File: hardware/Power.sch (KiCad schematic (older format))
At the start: 30 parts, among them J8 Batt, Q10 AO3401A, Q11 AO3400 (A09T), Q12 AO3401A, Q13 AO3400 (A09T), Q14 AO3400 (A09T), Q9 AO3400 (A09T), U1 TP4056, U3 DW-01, U8 HX9193-33GB

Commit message: Wrover fp
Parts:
- C15: LCSC (none) -> C14663
- C16, C22: LCSC (none) -> C15849
- C24, C25: LCSC (none) -> C134722
- D17, D18: LCSC (none) -> C72043
- D19: LCSC (none) -> C2480
- Q10, Q12: LCSC (none) -> C15127
- Q11, Q13, Q14, Q9: LCSC (none) -> C20917
- R47, R48, R52, R53: LCSC (none) -> C25804
- R49, R50, R51: LCSC (none) -> C22765
- R54: LCSC (none) -> C23179
- R55: LCSC (none) -> C21190
- R57: LCSC (none) -> C21189
- U1: LCSC (none) -> C16581
- U3: LCSC (none) -> C14213
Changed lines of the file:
@@
 F 7 "Eldon Vloerstaande kasten DW - DW01" H 6700 4050 50  0001 L BNN "Field7"
 F 8 "DW01" H 6700 4050 50  0001 L BNN "Field8"
+F 9 "C14213" H 6700 4050 50  0001 C CNN "LCSC"
 	1    6700 4050
 	1    0    0    -1
@@
 F 2 "Resistor_SMD:R_0603_1608Metric" V 5730 3800 50  0001 C CNN
 F 3 "~" H 5800 3800 50  0001 C CNN
+F 4 "C23179" H 5800 3800 50  0001 C CNN "LCSC"
 	1    5800 3800
 	0    1    1    0
@@
 F 2 "Capacitor_SMD:C_0603_1608Metric" H 6188 3800 50  0001 C CNN
 F 3 "~" H 6150 3950 50  0001 C CNN
+F 4 "C14663" H 6150 3950 50  0001 C CNN "LCSC"
 	1    6150 3950
 	1    0    0    -1
@@
 F 2 "Package_TO_SOT_SMD:SOT-23" H 6650 4775 50  0001 L CIN
 F 3 "http://www.aosmd.com/pdfs/datasheet/ao3400.pdf" H 6450 4850 50  0001 L CNN
+F 4 "C20917" H 6450 4850 50  0001 C CNN "LCSC"
 	1    6450 4850
 	0    1    1    0
@@
 F 2 "Package_TO_SOT_SMD:SOT-23" H 7100 4775 50  0001 L CIN
 F 3 "http://www.aosmd.com/pdfs/datasheet/ao3400.pdf" H 6900 4850 50  0001 L CNN
+F 4 "C20917" H 6900 4850 50  0001 C CNN "LCSC"
 	1    6900 4850
 	0    -1   1    0
@@
 F 2 "Resistor_SMD:R_0603_1608Metric" V 7130 4350 50  0001 C CNN
 F 3 "~" H 7200 4350 50  0001 C CNN
+F 4 "C21190" H 7200 4350 50  0001 C CNN "LCSC"
 	1    7200 4350
 	-1   0    0    1
@@
 F 2 "Diode_SMD:D_SMA" H 3600 2500 50  0001 C CNN
 F 3 "https://lcsc.com/product-detail/Schottky-Barrier-Diodes-SBD_SS34_C183891.html" H 3600 2500 50  0001 C CNN
+F 4 "C2480" H 3600 2500 50  0001 C CNN "LCSC"
 	1    3600 2500
 	-1   0    0    1
@@
 F 2 "Package_TO_SOT_SMD:SOT-23" H 5350 2425 50  0001 L CIN
 F 3 "http://www.aosmd.com/pdfs/datasheet/AO3401A.pdf" H 5150 2500 50  0001 L CNN
+F 4 "C15127" H 5150 2500 50  0001 C CNN "LCSC"
 	1    5150 2500
 	0    -1   -1   0
@@
 F 2 "Package_TO_SOT_SMD:SOT-23" H 5750 2425 50  0001 L CIN
 F 3 "http://www.aosmd.com/pdfs/datasheet/AO3401A.pdf" H 5550 2500 50  0001 L CNN
+F 4 "C15127" H 5550 2500 50  0001 C CNN "LCSC"
 	1    5550 2500
 	0    1    -1   0
@@
 F 2 "Resistor_SMD:R_0603_1608Metric" V 4930 2700 50  0001 C CNN
 F 3 "~" H 5000 2700 50  0001 C CNN
+F 4 "C25804" H 5000 2700 50  0001 C CNN "LCSC"
 	1    5000 2700
 	0    1    -1   0
@@
 F 2 "Package_SO:SOIC-8-1EP_3.9x4.9mm_P1.27mm_EP2.29x3mm" H 3600 4150 60  0001 C CNN
 F 3 "https://dlnmh9ip6v2uc.cloudfront.net/datasheets/Prototyping/TP4056.pdf" H 3600 4150 60  0001 C CNN
+F 4 "C16581" H 3600 4150 50  0001 C CNN "LCSC"
 	1    3600 4150
 	1    0    0    -1
@@
 F 2 "Resistor_SMD:R_0603_1608Metric" V 4030 4450 50  0001 C CNN
 F 3 "~" H 4100 4450 50  0001 C CNN
+F 4 "C22765" H 4100 4450 50  0001 C CNN "LCSC"
 	1    4100 4450
 	1    0    0    -1
@@
 F 2 "LED_SMD:LED_0603_1608Metric" H 2550 4500 50  0001 C CNN
 F 3 "~" H 2550 4500 50  0001 C CNN
+F 4 "C72043" H 2550 4500 50  0001 C CNN "LCSC"
 	1    2550 4500
 	-1   0    0    1
@@
 F 2 "LED_SMD:LED_0603_1608Metric" H 2550 4600 50  0001 C CNN
 F 3 "~" H 2550 4600 50  0001 C CNN
+F 4 "C72043" H 2550 4600 50  0001 C CNN "LCSC"
 	1    2550 4600
 	-1   0    0    1
@@
 F 2 "Resistor_SMD:R_0603_1608Metric" V 2930 4450 50  0001 C CNN
 F 3 "~" H 3000 4450 50  0001 C CNN
+F 4 "C22765" H 3000 4450 50  0001 C CNN "LCSC"
 	1    3000 4450
 	-1   0    0    -1
@@
 F 2 "Resistor_SMD:R_0603_1608Metric" V 2830 4350 50  0001 C CNN
 F 3 "~" H 2900 4350 50  0001 C CNN
+F 4 "C22765" H 2900 4350 50  0001 C CNN "LCSC"
 	1    2900 4350
 	1    0    0    -1
@@
 F 2 "Resistor_SMD:R_0603_1608Metric" V 2680 3850 50  0001 C CNN
 F 3 "~" H 2750 3850 50  0001 C CNN
+F 4 "C25804" H 2750 3850 50  0001 C CNN "LCSC"
 	1    2750 3850
 	1    0    0    -1
@@
 F 2 "Package_TO_SOT_SMD:SOT-23" H 2500 3875 50  0001 L CIN
 F 3 "http://www.aosmd.com/pdfs/datasheet/ao3400.pdf" H 2300 3950 50  0001 L CNN
+F 4 "C20917" H 2300 3950 50  0001 C CNN "LCSC"
 	1    2300 3950
 	0    1    -1   0
@@
 F 2 "Resistor_SMD:R_0603_1608Metric" V 1880 4000 50  0001 C CNN
 F 3 "~" H 1950 4000 50  0001 C CNN
+F 4 "C25804" H 1950 4000 50  0001 C CNN "LCSC"
 	1    1950 4000
 	1    0    0    -1
@@
 F 2 "Capacitor_SMD:C_0603_1608Metric" H 9038 5250 50  0001 C CNN
 F 3 "~" H 9000 5400 50  0001 C CNN
+F 4 "C15849" H 9000 5400 50  0001 C CNN "LCSC"
 	1    9000 5400
 	0    -1   1    0
@@
 F 2 "Capacitor_SMD:C_0603_1608Metric" H 10138 5250 50  0001 C CNN
 F 3 "~" H 10100 5400 50  0001 C CNN
+F 4 "C15849" H 10100 5400 50  0001 C CNN "LCSC"
 	1    10100 5400
 	0    -1   1    0
@@
 F 2 "Package_TO_SOT_SMD:SOT-23" H 5350 4475 50  0001 L CIN
 F 3 "http://www.aosmd.com/pdfs/datasheet/ao3400.pdf" H 5150 4550 50  0001 L CNN
+F 4 "C20917" H 5150 4550 50  0001 C CNN "LCSC"
 	1    5150 4550
 	-1   0    0    -1
@@
 F 2 "Resistor_SMD:R_0603_1608Metric" V 5380 4200 50  0001 C CNN
 F 3 "~" H 5450 4200 50  0001 C CNN
+F 4 "C25804" H 5450 4200 50  0001 C CNN "LCSC"
 	1    5450 4200
 	-1   0    0    1
@@
 F 2 "Capacitor_SMD:CP_Elec_5x5.4" H 9488 4300 50  0001 C CNN
 F 3 "~" H 9450 4450 50  0001 C CNN
+F 4 "C134722" H 9450 4450 50  0001 C CNN "LCSC"
 	1    9450 4450
 	1    0    0    -1
@@
 F 2 "Capacitor_SMD:CP_Elec_5x5.4" H 9938 4300 50  0001 C CNN
 F 3 "~" H 9900 4450 50  0001 C CNN
+F 4 "C134722" H 9900 4450 50  0001 C CNN "LCSC"
 	1    9900 4450
 	1    0    0    -1
@@
 F 2 "Resistor_SMD:R_0603_1608Metric" V 4280 4450 50  0001 C CNN
 F 3 "~" H 4350 4450 50  0001 C CNN
+F 4 "C21189" H 4350 4450 50  0001 C CNN "LCSC"
 	1    4350 4450
 	1    0    0    -1

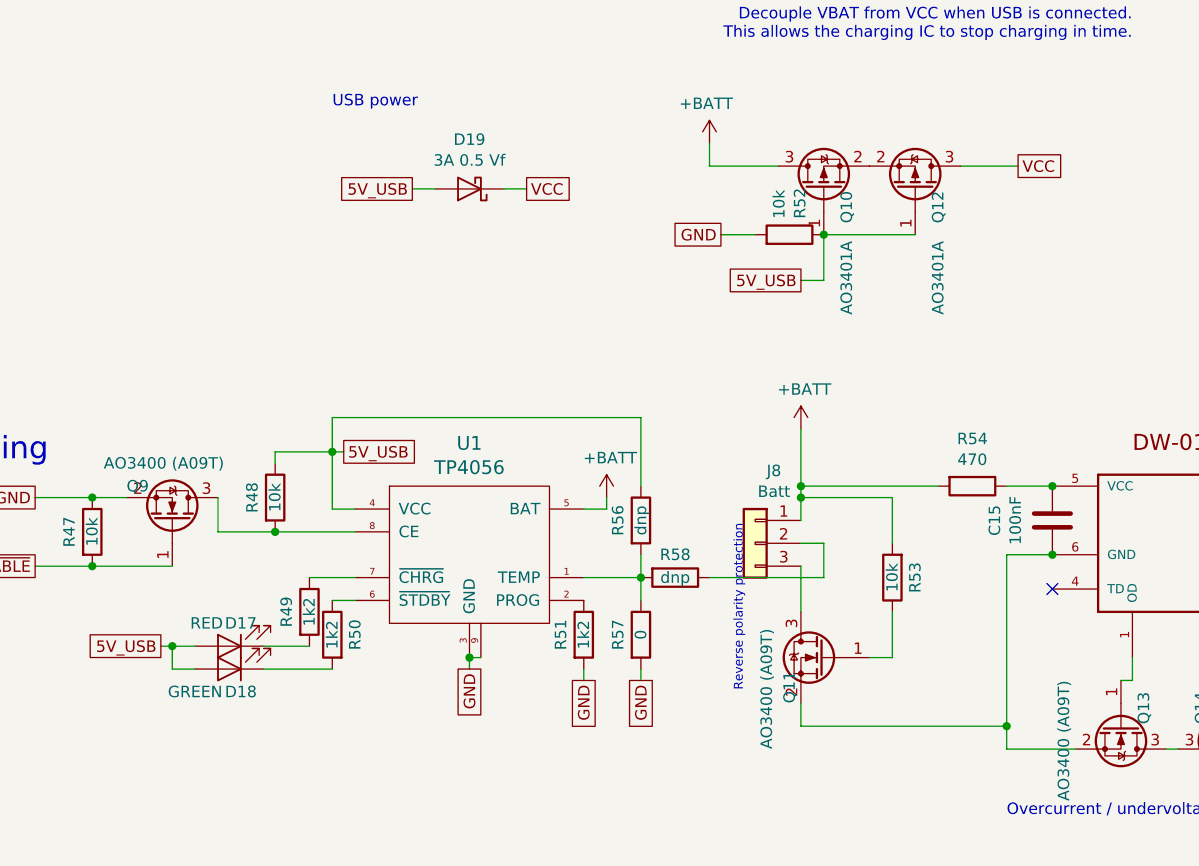
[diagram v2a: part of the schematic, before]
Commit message: Changed connectors to smd and added powerswitch
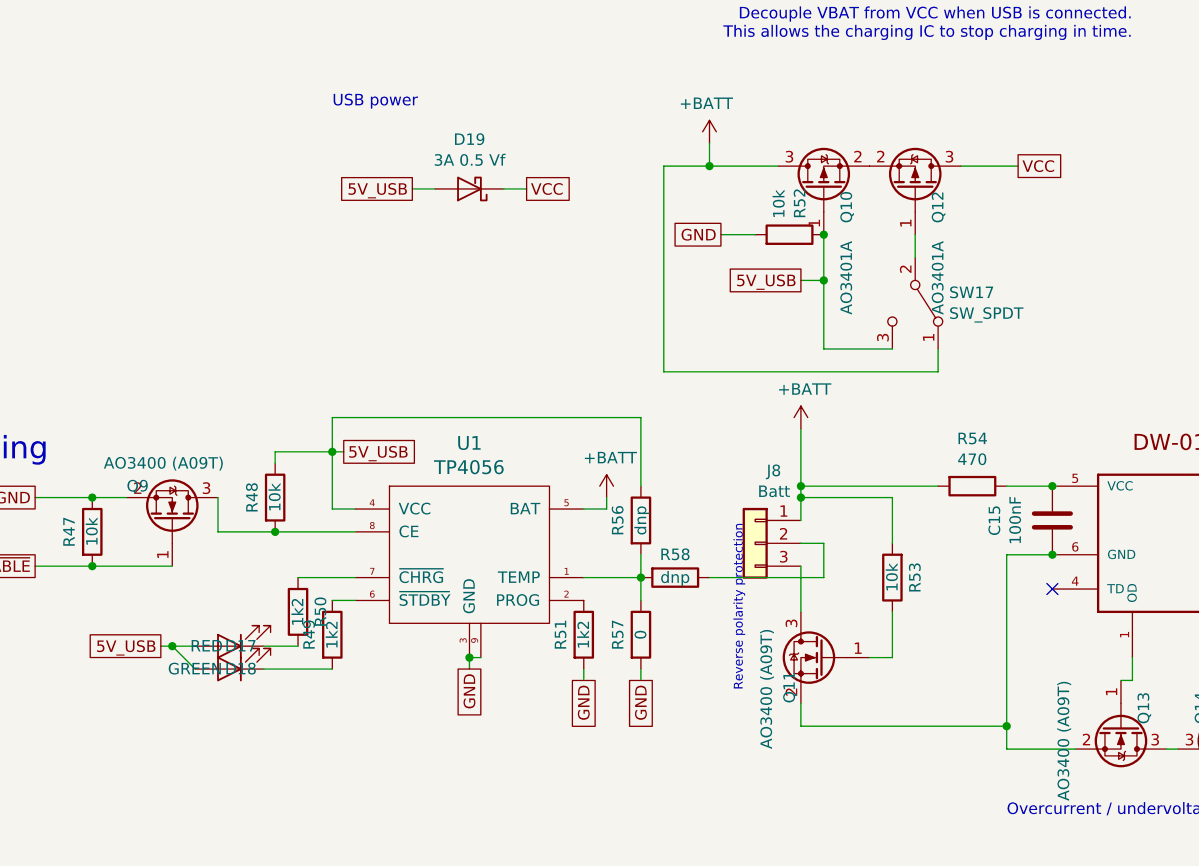
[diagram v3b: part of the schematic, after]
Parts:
- added SW17: SW_SPDT, switch:sk-3296s, symbol Switch:SW_SPDT
- J8: footprint Connector_JST:JST_PH_B3B-PH-K_1x03_P2.00mm_Vertical -> Connector_JST:JST_PH_B3B-PH-SM4-TB_1x03-1MP_P2.00mm_Vertical
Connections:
- net +BATT: now also SW17.1 (A)
- net 5V_USB: now also SW17.3 (C); no longer Q12.1 (G)
- net at U1.6 (~STDBY): now also R49.1; no longer R50.1
- net at U1.7 (~CHRG): now also R50.1; no longer R49.1
- new net: Q12.1 (G), SW17.2 (B)
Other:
- moved on the sheet: D17, D18, R49, R50
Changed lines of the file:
@@
 	0    1    -1   0
 $EndComp
-Wire Wire Line
-	5150 2700 5550 2700
 Text GLabel 6000 2400 2    50   UnSpc ~ 0
 VCC
@@
 L Device:LED D?
 U 1 1 5E4683D9
-P 2550 4500
+P 2550 4600
 AR Path="/5E4683D9" Ref="D?"  Part="1"
 AR Path="/5E4377A8/5E4683D9" Ref="D?"  Part="1"
 AR Path="/5E464BBE/5E4683D9" Ref="D17"  Part="1"
-F 0 "D17" H 2500 4400 50  0000 C CNN
-F 1 "RED" H 2650 4400 50  0000 C CNN
+F 0 "D17" H 2500 4500 50  0000 C CNN
+F 1 "RED" H 2650 4500 50  0000 C CNN
+F 2 "LED_SMD:LED_0603_1608Metric" H 2550 4600 50  0001 C CNN
+F 3 "~" H 2550 4600 50  0001 C CNN
+F 4 "C72043" H 2550 4600 50  0001 C CNN "LCSC"
+	1    2550 4600
+	-1   0    0    1
+$EndComp
+$Comp
+L Device:LED D?
+U 1 1 5E4683DF
+P 2550 4500
+AR Path="/5E4683DF" Ref="D?"  Part="1"
+AR Path="/5E4377A8/5E4683DF" Ref="D?"  Part="1"
+AR Path="/5E464BBE/5E4683DF" Ref="D18"  Part="1"
+F 0 "D18" H 2500 4600 50  0000 C CNN
+F 1 "GREEN" H 2700 4600 50  0000 C CNN
 F 2 "LED_SMD:LED_0603_1608Metric" H 2550 4500 50  0001 C CNN
 F 3 "~" H 2550 4500 50  0001 C CNN
@@
 	-1   0    0    1
 $EndComp
-$Comp
-L Device:LED D?
-U 1 1 5E4683DF
-P 2550 4600
-AR Path="/5E4683DF" Ref="D?"  Part="1"
-AR Path="/5E4377A8/5E4683DF" Ref="D?"  Part="1"
-AR Path="/5E464BBE/5E4683DF" Ref="D18"  Part="1"
-F 0 "D18" H 2500 4700 50  0000 C CNN
-F 1 "GREEN" H 2700 4700 50  0000 C CNN
-F 2 "LED_SMD:LED_0603_1608Metric" H 2550 4600 50  0001 C CNN
-F 3 "~" H 2550 4600 50  0001 C CNN
-F 4 "C72043" H 2550 4600 50  0001 C CNN "LCSC"
-	1    2550 4600
-	-1   0    0    1
-$EndComp
-Wire Wire Line
-	3000 4300 3100 4300
 Wire Wire Line
 	4200 3850 4200 3900
@@
 L Device:R R?
 U 1 1 5E4683E7
-P 3000 4450
+P 2850 4350
 AR Path="/5E4683E7" Ref="R?"  Part="1"
 AR Path="/5E4377A8/5E4683E7" Ref="R?"  Part="1"
 AR Path="/5E464BBE/5E4683E7" Ref="R50"  Part="1"
-F 0 "R50" V 2900 4450 50  0000 C CNN
+F 0 "R50" V 2750 4350 50  0000 C CNN
+F 1 "1k2" V 2850 4350 50  0000 C CNN
+F 2 "Resistor_SMD:R_0603_1608Metric" V 2780 4350 50  0001 C CNN
+F 3 "~" H 2850 4350 50  0001 C CNN
+F 4 "C22765" H 2850 4350 50  0001 C CNN "LCSC"
+	1    2850 4350
+	-1   0    0    -1
+$EndComp
+$Comp
+L Device:R R?
+U 1 1 5E4683ED
+P 3000 4450
+AR Path="/5E4683ED" Ref="R?"  Part="1"
+AR Path="/5E4377A8/5E4683ED" Ref="R?"  Part="1"
+AR Path="/5E464BBE/5E4683ED" Ref="R49"  Part="1"
+F 0 "R49" V 2900 4450 50  0000 C CNN
 F 1 "1k2" V 3000 4450 50  0000 C CNN
 F 2 "Resistor_SMD:R_0603_1608Metric" V 2930 4450 50  0001 C CNN
@@
 F 4 "C22765" H 3000 4450 50  0001 C CNN "LCSC"
 	1    3000 4450
-	-1   0    0    -1
-$EndComp
-$Comp
-L Device:R R?
-U 1 1 5E4683ED
-P 2900 4350
-AR Path="/5E4683ED" Ref="R?"  Part="1"
-AR Path="/5E4377A8/5E4683ED" Ref="R?"  Part="1"
-AR Path="/5E464BBE/5E4683ED" Ref="R49"  Part="1"
-F 0 "R49" V 2800 4350 50  0000 C CNN
-F 1 "1k2" V 2900 4350 50  0000 C CNN
-F 2 "Resistor_SMD:R_0603_1608Metric" V 2830 4350 50  0001 C CNN
-F 3 "~" H 2900 4350 50  0001 C CNN
-F 4 "C22765" H 2900 4350 50  0001 C CNN "LCSC"
-	1    2900 4350
-	1    0    0    -1
-$EndComp
-Wire Wire Line
-	2900 4200 3100 4200
-Wire Wire Line
-	2700 4500 2900 4500
-Wire Wire Line
-	3000 4600 2700 4600
+	1    0    0    -1
+$EndComp
+Wire Wire Line
+	2700 4600 3000 4600
+Wire Wire Line
+	2850 4500 2700 4500
 Text GLabel 2250 4500 0    50   UnSpc ~ 0
 5V_USB
 Wire Wire Line
-	2300 4500 2300 4600
-Wire Wire Line
-	2300 4600 2400 4600
-Wire Wire Line
 	2300 4500 2400 4500
+Wire Wire Line
+	2300 4500 2400 4600
 Wire Wire Line
 	2250 4500 2300 4500
@@
 F 0 "J8" H 4768 4367 50  0000 C CNN
 F 1 "Batt" H 4768 4276 50  0000 C CNN
-F 2 "Connector_JST:JST_PH_B3B-PH-K_1x03_P2.00mm_Vertical" H 4850 4050 50  0001 C CNN
+F 2 "Connector_JST:JST_PH_B3B-PH-SM4-TB_1x03-1MP_P2.00mm_Vertical" H 4850 4050 50  0001 C CNN
 F 3 "~" H 4850 4050 50  0001 C CNN
 	1    4850 4050
@@
 Wire Wire Line
 	7100 4950 7100 4850
+$Comp
+L Switch:SW_SPDT SW17
+U 1 1 5E7C5A42
+P 5550 3000
+F 0 "SW17" V 5504 3148 50  0000 L CNN
+F 1 "SW_SPDT" V 5595 3148 50  0000 L CNN
+F 2 "switch:sk-3296s" H 5550 3000 50  0001 C CNN
+F 3 "~" H 5550 3000 50  0001 C CNN
+	1    5550 3000
+	0    1    1    0
+$EndComp
+Wire Wire Line
+	5550 2800 5550 2700
+Wire Wire Line
+	5450 3200 5150 3200
+Wire Wire Line
+	5150 3200 5150 2900
+Connection ~ 5150 2900
+Wire Wire Line
+	5650 3200 5650 3300
+Wire Wire Line
+	5650 3300 4450 3300
+Wire Wire Line
+	4450 3300 4450 2400
+Wire Wire Line
+	4450 2400 4650 2400
+Connection ~ 4650 2400
+Wire Wire Line
+	3100 4200 2850 4200
+Wire Wire Line
+	3000 4300 3100 4300
 $EndSCHEMATC

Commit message: Production data rev4
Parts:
- SW17: LCSC (none) -> C319020
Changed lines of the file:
@@
 F 2 "switch:sk-3296s" H 5550 3000 50  0001 C CNN
 F 3 "~" H 5550 3000 50  0001 C CNN
+F 4 " C319020" H 5550 3000 50  0001 C CNN "LCSC"
 	1    5550 3000
 	0    1    1    0

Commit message: Updated production files: - vias in 8-pin female header - fixed some text elements - added testpoint for FLASH
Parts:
- SW17: LCSC C319020 -> (none)
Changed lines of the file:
@@
 F 2 "switch:sk-3296s" H 5550 3000 50  0001 C CNN
 F 3 "~" H 5550 3000 50  0001 C CNN
-F 4 " C319020" H 5550 3000 50  0001 C CNN "LCSC"
 	1    5550 3000
 	0    1    1    0

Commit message: Rev5 schematic changes and pcb cleanup
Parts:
- R49, R50: value 1k2 -> 10k; LCSC C22765 -> (none)
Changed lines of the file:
@@
 AR Path="/5E464BBE/5E4683E7" Ref="R50"  Part="1"
 F 0 "R50" V 2750 4350 50  0000 C CNN
-F 1 "1k2" V 2850 4350 50  0000 C CNN
+F 1 "10k" V 2850 4350 50  0000 C CNN
 F 2 "Resistor_SMD:R_0603_1608Metric" V 2780 4350 50  0001 C CNN
 F 3 "~" H 2850 4350 50  0001 C CNN
-F 4 "C22765" H 2850 4350 50  0001 C CNN "LCSC"
+F 4 "" H 2850 4350 50  0001 C CNN "LCSC"
 	1    2850 4350
 	-1   0    0    -1
@@
 AR Path="/5E464BBE/5E4683ED" Ref="R49"  Part="1"
 F 0 "R49" V 2900 4450 50  0000 C CNN
-F 1 "1k2" V 3000 4450 50  0000 C CNN
+F 1 "10k" V 3000 4450 50  0000 C CNN
 F 2 "Resistor_SMD:R_0603_1608Metric" V 2930 4450 50  0001 C CNN
 F 3 "~" H 3000 4450 50  0001 C CNN
-F 4 "C22765" H 3000 4450 50  0001 C CNN "LCSC"
+F 4 "" H 3000 4450 50  0001 C CNN "LCSC"
 	1    3000 4450
 	1    0    0    -1

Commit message: Fixed BOM lines
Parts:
- R49, R50: LCSC (none) -> C25804
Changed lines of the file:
@@
 F 2 "Resistor_SMD:R_0603_1608Metric" V 2780 4350 50  0001 C CNN
 F 3 "~" H 2850 4350 50  0001 C CNN
-F 4 "" H 2850 4350 50  0001 C CNN "LCSC"
+F 4 "C25804" H 2850 4350 50  0001 C CNN "LCSC"
 	1    2850 4350
 	-1   0    0    -1
@@
 F 2 "Resistor_SMD:R_0603_1608Metric" V 2930 4450 50  0001 C CNN
 F 3 "~" H 3000 4450 50  0001 C CNN
-F 4 "" H 3000 4450 50  0001 C CNN "LCSC"
+F 4 "C25804" H 3000 4450 50  0001 C CNN "LCSC"
 	1    3000 4450
 	1    0    0    -1

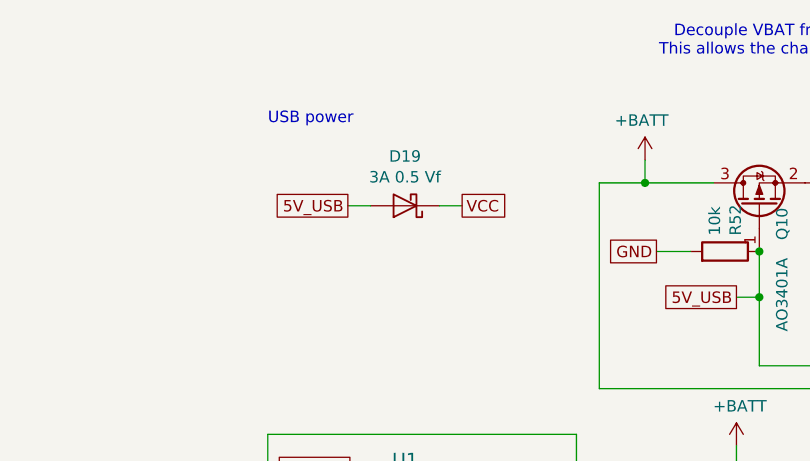
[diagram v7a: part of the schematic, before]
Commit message: Fixed 3.3V rail to led drivers. Switched to 2A diode
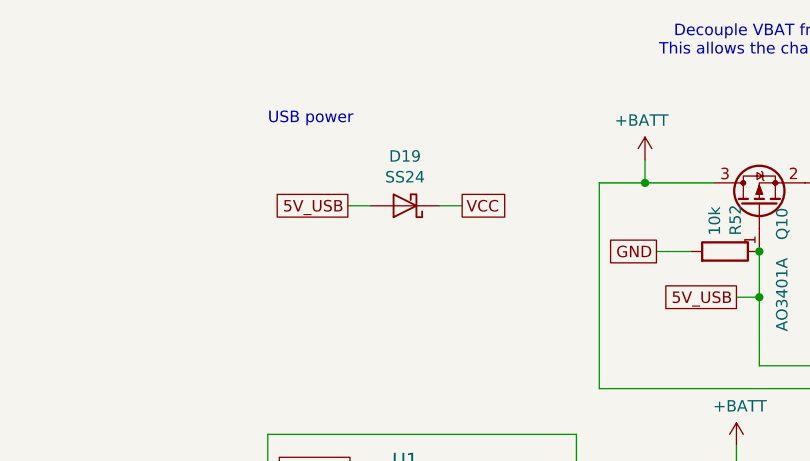
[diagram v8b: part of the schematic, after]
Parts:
- D19: value 3A 0.5 Vf -> SS24; LCSC C2480 -> C181203
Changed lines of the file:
@@
 AR Path="/5E464BBE/5E44BF09" Ref="D19"  Part="1"
 F 0 "D19" H 3600 2284 50  0000 C CNN
-F 1 "3A 0.5 Vf" H 3600 2375 50  0000 C CNN
+F 1 "SS24" H 3600 2375 50  0000 C CNN
 F 2 "Diode_SMD:D_SMA" H 3600 2500 50  0001 C CNN
 F 3 "https://lcsc.com/product-detail/Schottky-Barrier-Diodes-SBD_SS34_C183891.html" H 3600 2500 50  0001 C CNN
-F 4 "C2480" H 3600 2500 50  0001 C CNN "LCSC"
+F 4 "C181203" H 3600 2500 50  0001 C CNN "LCSC"
 	1    3600 2500
 	-1   0    0    1
